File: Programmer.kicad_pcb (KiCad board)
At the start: 2 copper layers, 76.2 x 50.8 mm, 58 parts, among them CON1 USB_OTG, M1 ESP-12E, P1 Test, P3 CONN_12, Q1 MMBT3904, Q2 MMBT3906, Q3 MMBT3904, SW1 Upload, SW2 RESET, U1 AP2112K-3.3, U10 NC7SB3157, U2 23LC1024, U3 74LVC2T45, U4 74LVC2T45, U5 74LVC2T45, U6 74LVC2T45, U7 AAT1230, U8 CP2104, U9 MCP23S08

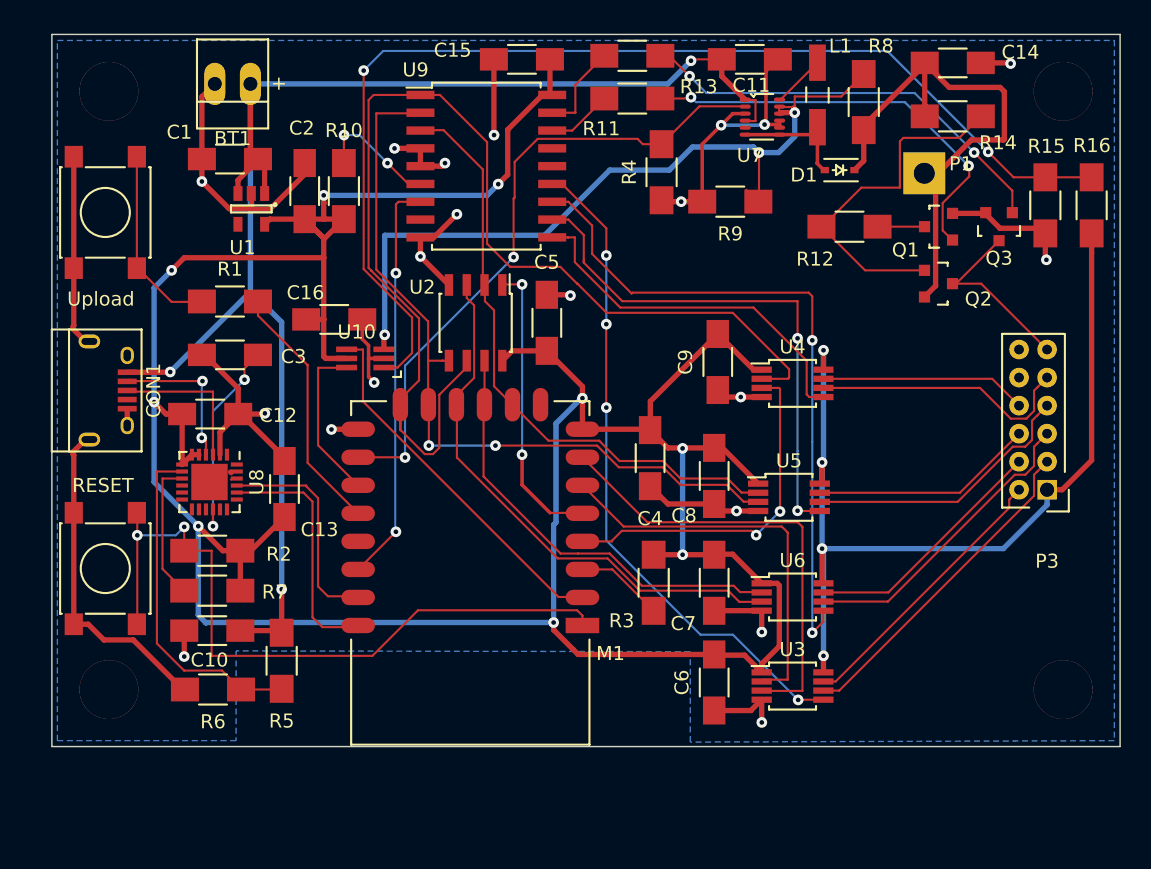
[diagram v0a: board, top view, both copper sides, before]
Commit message: Re-layout Update V00B
Multiple changes to the schematic and PCB component placement, complete
re-route of PCB.
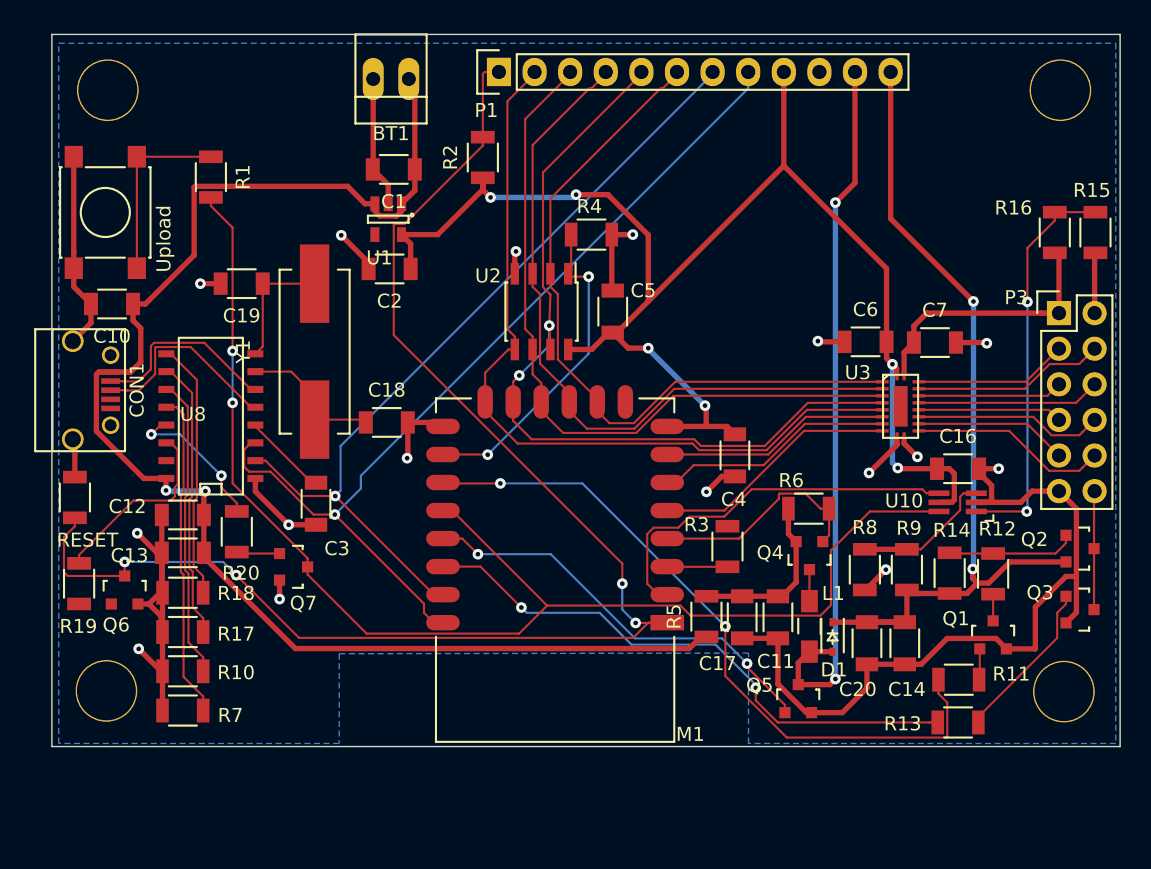
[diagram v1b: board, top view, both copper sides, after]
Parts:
- removed C15: 0.1. µF, Capacitors_SMD:C_1206_HandSoldering
- removed C8, C9: 0.1 µF, Capacitors_SMD:C_1206_HandSoldering
- removed the REF** at (54.9, 40.4)
- removed the REF** at (54.9, 83.1)
- removed the REF** at (122.9, 40.4)
- removed the REF** at (122.9, 83.1)
- removed U4, U5, U6: 74LVC2T45, Housings_SSOP:MSOP-8_3x3mm_Pitch0.65mm
- removed U7: AAT1230, Uprogrammer FPs:12-TFSOJ
- removed U9: MCP23S08, Housings_SOIC:SOIC-18_7.5x11.6mm_Pitch1.27mm
- added C17: 100 µF, Capacitors_SMD:C_1206, F.Cu at (100.0, 77.9)
- added C18: 22 pF, Capacitors_SMD:C_1206, F.Cu at (74.7, 64.0)
- added C19: 22 pF, Capacitors_SMD:C_1206, F.Cu at (64.3, 54.1)
- added C20: 0.1 µF, Capacitors_SMD:C_1206, F.Cu at (109.0, 79.8)
- added Q4: BSS84, Housings_SOT-23_SOT-143_TSOT-6:SOT-23, F.Cu at (104.8, 73.5)
- added Q5: BSS138L, Housings_SOT-23_SOT-143_TSOT-6:SOT-23, F.Cu at (104.0, 83.7)
- added Q6: MMBT3904, Housings_SOT-23_SOT-143_TSOT-6:SOT-23, F.Cu at (56.0, 75.9)
- added Q7: MMBT3904, Housings_SOT-23_SOT-143_TSOT-6:SOT-23, F.Cu at (68.0, 74.3)
- added R17: 1K, Resistors_SMD:R_1206, F.Cu at (60.1, 79.0)
- added R18: 1K, Resistors_SMD:R_1206, F.Cu at (60.1, 76.2)
- added R19: 10K, Resistors_SMD:R_1206, F.Cu at (52.8, 75.5)
- added R20: 10K, Resistors_SMD:R_1206, F.Cu at (64.0, 71.8)
- added REF**: MountingHole_4mm, Mounting_Holes:MountingHole_4mm, F.Cu at (122.8, 40.3)
- added REF**: MountingHole_4mm, Mounting_Holes:MountingHole_4mm, F.Cu at (123.0, 83.2)
- added REF**: MountingHole_4mm, Mounting_Holes:MountingHole_4mm, F.Cu at (54.7, 83.2)
- added REF**: MountingHole_4mm, Mounting_Holes:MountingHole_4mm, F.Cu at (54.8, 40.3)
- added Y1: 12 Mhz, Crystals:Crystal_HC49-SD_SMD, F.Cu at (69.5, 59.0)
- BT1: value + -> BATTERY
- C1, C10, C11, C13, C14, C16, C2, C4, C5, C6, C7: footprint Capacitors_SMD:C_1206_HandSoldering -> Capacitors_SMD:C_1206
- C12: value 1 µF -> 10 µF; footprint Capacitors_SMD:C_1206_HandSoldering -> Capacitors_SMD:C_1206
- C3: value 4.7 µF -> 0.1 µF; footprint Capacitors_SMD:C_1206_HandSoldering -> Capacitors_SMD:C_1206
- L1: footprint Choke_SMD:Choke_SMD_1206_Handsoldering -> Choke_SMD:Choke_SMD_1206_Standard
- P1: value Test -> CONN_01X12; footprint Measurement_Points:Measurement_Point_Square-TH_Big -> Socket_Strips:Socket_Strip_Straight_1x12
- P3: footprint Uprogrammer FPs:Header_Straight_2mm_2x06 -> Pin_Headers:Pin_Header_Straight_2x06
- R1, R11, R12, R13, R14, R15, R16, R2, R3, R4, R8, R9: footprint Resistors_SMD:R_1206_HandSoldering -> Resistors_SMD:R_1206
- R10, R7: value 4.7K -> 1K; footprint Resistors_SMD:R_1206_HandSoldering -> Resistors_SMD:R_1206
- R5: value 24K -> 10; footprint Resistors_SMD:R_1206_HandSoldering -> Resistors_SMD:R_1206
- R6: value 47K -> 10K; footprint Resistors_SMD:R_1206_HandSoldering -> Resistors_SMD:R_1206
- SW2: footprint Buttons_Switches_SMD:SW_SPST_PTS645 -> Resistors_SMD:R_1206
- U3: value 74LVC2T45 -> FXMA108; footprint Housings_SSOP:MSOP-8_3x3mm_Pitch0.65mm -> Uprogrammer FPs:DQFN20
- U8: value CP2104 -> CH340G; footprint Housings_DFN_QFN:QFN-24-1EP_4x4mm_Pitch0.5mm -> SMD_Packages:SO-16-N
- moved R13 52.9 mm to (115.5, 85.4)
- moved R11 47.6 mm to (115.5, 82.3)
- moved C16 45.8 mm to (115.5, 67.3)
- moved R6 44.4 mm to (104.8, 70.2)
- moved U10 43.5 mm to (115.4, 69.7)
- moved C14 41.5 mm to (111.7, 79.8), turned to 270 degrees
- moved C11 39.9 mm to (102.6, 77.9), turned to 270 degrees
- moved L1 37.9 mm to (104.8, 78.5)
- moved R10 36.1 mm to (60.1, 81.8), turned to 0 degrees
- moved R2 34.0 mm to (81.5, 45.1), turned to 90 degrees
- moved R8 33.5 mm to (111.8, 74.5)
- moved D1 33.3 mm to (106.5, 79.3), turned to 270 degrees
- moved R14 32.6 mm to (114.8, 74.8), turned to 90 degrees
- moved P1 31.2 mm to (82.7, 39.0)
- moved R5 30.5 mm to (97.5, 77.8)
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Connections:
- C11 pad 1: +BATT -> /Vpf
- C12 pad 1: 3V3 -> +BATT
- C13 pad 1: 3V3 -> +BATT
- C7 pad 1: GND -> VEE
- C7 pad 2: 3V3 -> GND
- D1 pad 2: Net-(D1-Pad2) -> /Pulse
- L1 pad 2: Net-(D1-Pad2) -> /Pulse
- M1 pad 1: Net-(M1-Pad1) -> /~RST
- M1 pad 10: Net-(M1-Pad10) -> /MISO
- M1 pad 11: Net-(M1-Pad11) -> /IO2
- M1 pad 12: Net-(M1-Pad12) -> /SCK
- M1 pad 13: Net-(M1-Pad13) -> /IO3
- M1 pad 14: Net-(M1-Pad14) -> /MOSI
- M1 pad 16: /SetV -> Net-(M1-Pad16)
- M1 pad 19: Net-(M1-Pad19) -> /HVpulse
- M1 pad 4: Net-(M1-Pad4) -> /~HV
- P1 pad 1: VPP -> /~RST
- P3 pad 10: GND -> Net-(P3-Pad10)
- P3 pad 11: Net-(P3-Pad11) -> GND
- P3 pad 12: GND -> Net-(P3-Pad12)
- P3 pad 2: Net-(P3-Pad2) -> GND
- Q2 pad 3: Net-(P3-Pad11) -> Net-(P3-Pad12)
- Q3 pad 3: Net-(P3-Pad11) -> Net-(P3-Pad12)
- R10 pad 1: Net-(R10-Pad1) -> GND
- R10 pad 2: 3V3 -> Net-(R10-Pad2)
- R11 pad 2: Net-(R11-Pad2) -> Net-(M1-Pad17)
- R13 pad 2: Net-(R13-Pad2) -> Net-(M1-Pad20)
- R2 pad 2: Net-(M1-Pad1) -> /~RST
- R4 pad 2: /SetV -> Net-(M1-Pad16)
- R5 pad 1: Net-(R5-Pad1) -> +BATT
- R5 pad 2: +BATT -> /Vpf
- R6 pad 1: Net-(R5-Pad1) -> /~HV
- R6 pad 2: GND -> /Vpf
- R7 pad 1: Net-(R7-Pad1) -> GND
- R7 pad 2: 3V3 -> Net-(R7-Pad2)
- SW2 pad 2: Net-(M1-Pad1) -> /~RST
- U10 pad 6: Net-(M1-Pad17) -> Net-(M1-Pad18)
- U2 pad 1: Net-(M1-Pad5) -> Net-(M1-Pad16)
- U2 pad 2: Net-(M1-Pad10) -> /MISO
- U2 pad 3: Net-(M1-Pad12) -> /IO2
- U2 pad 5: Net-(M1-Pad13) -> /MOSI
- U2 pad 6: Net-(M1-Pad14) -> /SCK
- U2 pad 7: Net-(M1-Pad11) -> /IO3
- U3 pad 2: Net-(M1-Pad6) -> /MISO
- U3 pad 3: Net-(M1-Pad7) -> /IO2
- U3 pad 4: GND -> /SCK
- U3 pad 5: /D3 -> /IO3
- U3 pad 6: Net-(P3-Pad3) -> /MOSI
- U3 pad 7: Net-(P3-Pad2) -> Net-(M1-Pad7)
- U3 pad 8: VEE -> Net-(M1-Pad6)
- U8 pad 1: Net-(U8-Pad1) -> GND
- U8 pad 11: Net-(U8-Pad11) -> Net-(R10-Pad2)
- U8 pad 12: Net-(U8-Pad12) -> Net-(R7-Pad2)
- U8 pad 16: Net-(C3-Pad1) -> +BATT
- U8 pad 2: GND -> /TxD
- U8 pad 3: Net-(CON1-Pad3) -> /RxD
- U8 pad 4: Net-(CON1-Pad2) -> Net-(C3-Pad1)
- U8 pad 5: 3V3 -> Net-(CON1-Pad3)
- U8 pad 6: 3V3 -> Net-(CON1-Pad2)
- U8 pad 7: 3V3 -> Net-(C18-Pad1)
- U8 pad 8: Net-(R5-Pad1) -> Net-(C19-Pad1)
- U8 pad 9: Net-(R7-Pad1) -> Net-(R18-Pad2)
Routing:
- net 3V3: track 225.2 -> 105.4 mm, vias 9 -> 6
- net /~RST: track 0.00 -> 103.9 mm, vias 0 -> 4
- net Net-(M1-Pad14): track 83.2 -> 0.00 mm
- net Net-(M1-Pad18): track 18.1 -> 93.3 mm, vias 0 -> 2
- net /IO3: track 0.00 -> 59.1 mm, vias 0 -> 2
- net /MOSI: track 0.00 -> 57.0 mm
- net Net-(M1-Pad13): track 55.1 -> 0.00 mm, vias 2 -> 0
- net /SCK: track 0.00 -> 52.5 mm
- net Net-(R15-Pad2): track 80.3 -> 28.7 mm
- net /IO2: track 0.00 -> 51.6 mm
- net Net-(M1-Pad1): track 51.4 -> 0.00 mm, vias 2 -> 0
- net /MISO: track 0.00 -> 51.3 mm
- net /Pulse: track 0.00 -> 51.0 mm, vias 0 -> 2
- net /D2: track 48.5 -> 0.00 mm, vias 2 -> 0
- net VEE: track 67.4 -> 18.9 mm, vias 4 -> 0
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
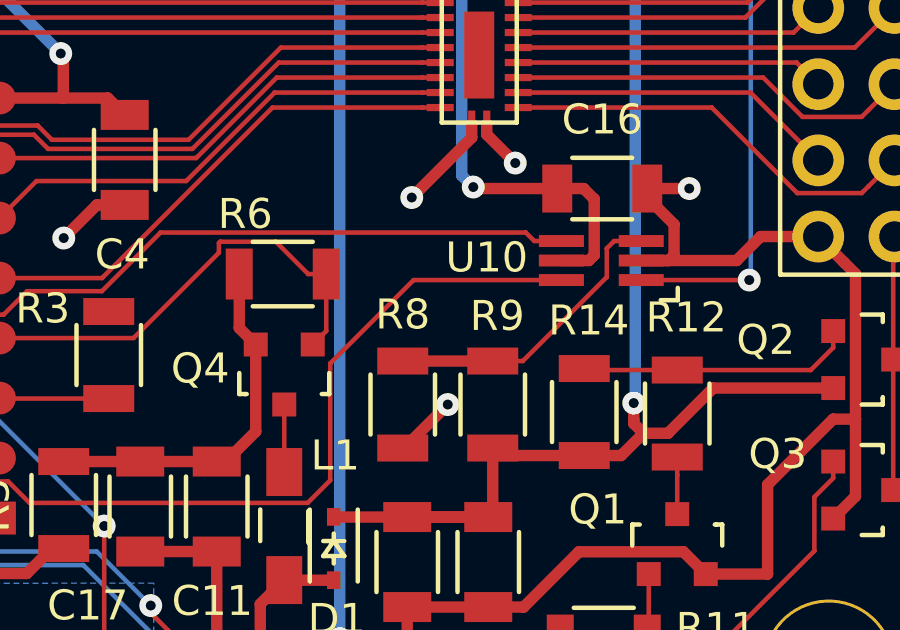
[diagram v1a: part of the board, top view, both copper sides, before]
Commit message: Hardware V00C
Design Update to start testing a lithium polimer cell as my power
source. Added a charge management IC that charges as well as supplies
system voltage.
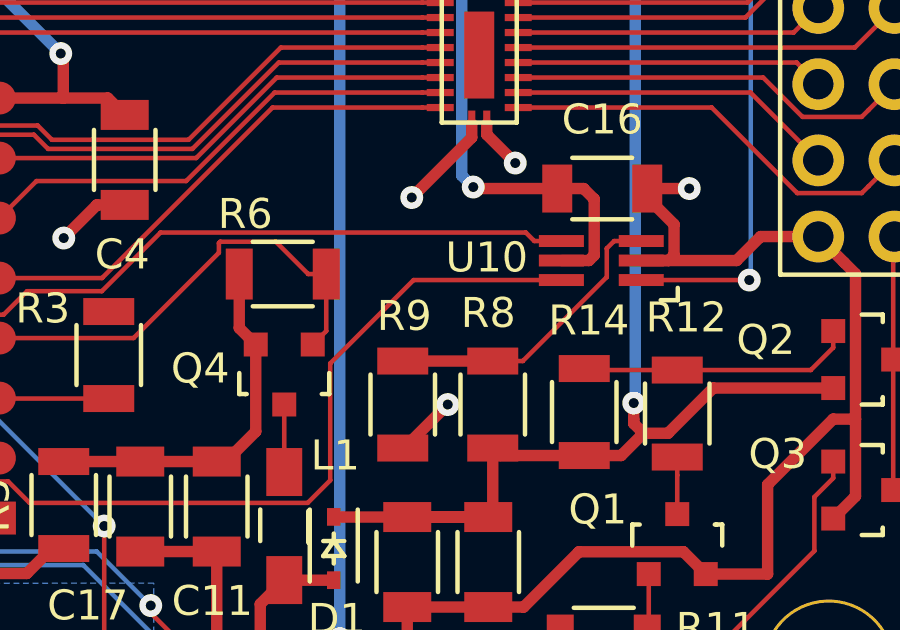
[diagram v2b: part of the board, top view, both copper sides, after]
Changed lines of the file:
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@@
     (links 159)
     (no_connects 3)
-    (area 50.759999 36.269999 127.060001 87.170001)
+    (area 41.794029 30.3726 147.541686 105.74316)
     (thickness 1.6)
     (drawings 8)
@@
     (tags "resistor 1206")
     (attr smd)
-    (fp_text reference R8 (at 3 -3 180) (layer F.SilkS)
+    (fp_text reference R8 (at 3.05 -0.15 180) (layer F.SilkS)
       (effects (font (size 1 1) (thickness 0.15)))
     )
@@
     (tags "resistor 1206")
     (attr smd)
-    (fp_text reference R9 (at -2.95 -3.15 360) (layer F.SilkS)
+    (fp_text reference R9 (at -2.95 -0.05 360) (layer F.SilkS)
       (effects (font (size 1 1) (thickness 0.15)))
     )
@@
   (segment (start 110.35 58.25) (end 110.35 59.431) (width 0.381) (layer F.Cu) (net 4))
   (segment (start 111.06659 60.14759) (end 111.06659 60.55) (width 0.381) (layer F.Cu) (net 4))
-  (segment (start 76.2 64) (end 76.2 66.5) (width 0.381) (layer F.Cu) (net 5) (status 400000))
+  (segment (start 76.2 64) (end 76.2 66.5) (width 0.381) (layer F.Cu) (net 5))
   (segment (start 76.2 66.6) (end 76.2 66.65) (width 0.381) (layer B.Cu) (net 5))
   (segment (start 76.15 66.55) (end 76.2 66.6) (width 0.381) (layer B.Cu) (net 5))
